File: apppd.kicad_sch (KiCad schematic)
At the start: 0 parts

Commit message: Added basic components from GPS
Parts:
- added C1, C9: 10uF, Resistor_SMD:R_0805_2012Metric_Pad1.20x1.40mm_HandSolder, symbol Device:C
- added C10, C12, C4, C5, C6, C7, C8: 100nF, Resistor_SMD:R_0805_2012Metric_Pad1.20x1.40mm_HandSolder, symbol Device:C
- added C11, C2, C3: 1uF, Resistor_SMD:R_0805_2012Metric_Pad1.20x1.40mm_HandSolder, symbol Device:C
- added D1, D2: LED, Package_TO_SOT_SMD:SOT-23, symbol Device:LED
- added F1: 100mA Polyfuse, Capacitor_SMD:C_0603_1608Metric_Pad1.08x0.95mm_HandSolder, symbol Device:Polyfuse
- added FB1: FerriteBead, Capacitor_SMD:C_0603_1608Metric_Pad1.08x0.95mm_HandSolder, symbol Device:FerriteBead_Small
- added J1: Conn_SWD, Connector_PinHeader_2.54mm:PinHeader_1x04_P2.54mm_Vertical, symbol Connector_Generic:Conn_01x04
- added J4: 2601-1102, apppd:WAGO-2601-1102, symbol telemetry:2601-1102
- added J5: USB_C_Receptacle_USB2.0_16P, apppd:USB-C-SMD_TYPE-C-16PIN-2MD-073, symbol Connector:USB_C_Receptacle_USB2.0_16P
- added Q1, Q2: AO3400A, Package_TO_SOT_SMD:SOT-23, symbol Transistor_FET:AO3400A
- added R1: 10k, Resistor_SMD:R_0805_2012Metric_Pad1.20x1.40mm_HandSolder, symbol Device:R
- added R10, R7, R8, R9: R_US, Resistor_THT:R_Array_SIP4, symbol Device:R_US
- added R2, R3: 5.1k, Resistor_SMD:R_0805_2012Metric_Pad1.20x1.40mm_HandSolder, symbol Device:R
- added R4, R5, R6: 10k, Resistor_SMD:R_0805_2012Metric_Pad1.20x1.40mm_HandSolder, symbol Device:R_US
- added SW1: NRST, apppd:SW-SMD_L3.9-W3.0-P4.45, symbol EasyEDA:TS-1088-AR02016
- added SW2: BOOT0, apppd:SW-SMD_L3.9-W3.0-P4.45, symbol EasyEDA:TS-1088-AR02016
- added TP5: CAN+, TestPoint:TestPoint_THTPad_D2.0mm_Drill1.0mm, symbol Connector:TestPoint
- added TP6: CAN-, TestPoint:TestPoint_THTPad_D2.0mm_Drill1.0mm, symbol Connector:TestPoint
- added TP7: +3V3, TestPoint:TestPoint_THTPad_D2.0mm_Drill1.0mm, symbol Connector:TestPoint
- added TP8: VIN_LDO, TestPoint:TestPoint_THTPad_D2.0mm_Drill1.0mm, symbol Connector:TestPoint
- added TP9: GND, TestPoint:TestPoint_THTPad_D2.0mm_Drill1.0mm, symbol Connector:TestPoint
- added U1: AP2112K-3.3, Package_TO_SOT_SMD:SOT-23-5_HandSoldering, symbol Regulator_Linear:AP2112K-3.3
- added U2: STM32F072CBTx, Package_QFP:LQFP-48_7x7mm_P0.5mm, symbol MCU_ST_STM32F0:STM32F072CBTx
- added U3: USBLC6-2SC6, Package_TO_SOT_SMD:SOT-23-6, symbol Power_Protection:USBLC6-2SC6
- added U4: TCAN337, Package_SO:SOIC-8_3.9x4.9mm_P1.27mm, symbol Interface_CAN_LIN:TCAN337
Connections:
- new net: J5.A5 (CC1), R2.1
- new net: J5.B5 (CC2), R3.1
- new net: FB1.2, U2.9 (VDDA)
- new net +3V3: C11.1, C12.2, C3.1, C4.2, C5.2, C6.2, C7.2, C8.2, C9.2, FB1.1, J1.4 (Pin_4), R4.1, R5.1, SW2.1, TP7.1, U1.5 (VOUT), U2.1 (VBAT), U2.24 (VDD), U2.36 (VDDIO2), U2.48 (VDD), U4.3 (VCC)
- new net BOOT0: R1.2, SW2.2, U2.44 (BOOT0)
- new net CAN+: J4.1 (1_1), J4.2 (1_2), TP5.1, U4.7 (CANH)
- new net CAN-: J4.3 (2_1), J4.4 (2_2), TP6.1, U4.6 (CANL)
- new net D+: U2.33 (PA12), U3.4 (I/O2)
- new net D-: U2.32 (PA11), U3.6 (I/O1)
- new net ETB_FET: U2.21 (PB10)
- new net FLT_CAN: R5.2, U2.18 (PB0), U4.5 (FAULT)
- new net GND: C1.1, C10.1, C11.2, C12.1, C2.2, C3.2, C4.1, C5.1, C6.1, C7.1, C8.1, C9.1, J1.1 (Pin_1), J5.A1 (GND), J5.A12 (GND), J5.B1 (GND), J5.B12 (GND), J5.SH (SHIELD), R1.1, R2.2, R3.2, R6.2, SW1.1, TP9.1, U1.2 (GND), U2.23 (VSS), U2.35 (VSS), U2.47 (VSS), U2.8 (VSSA), U3.2 (GND), U4.2 (GND)
- new net IGN_FET: U2.22 (PB11)
- new net NRST: C10.2, SW1.2, U2.7 (NRST)
- new net RXD_CAN: U2.45 (PB8), U4.4 (RXD)
- new net SIL_CAN: R6.1, U2.19 (PB1), U4.8 (S)
- new net SWCLK: J1.2 (Pin_2), U2.37 (PA14)
- new net SWDIO: J1.3 (Pin_3), U2.34 (PA13)
- new net TXD_CAN: R4.2, U2.46 (PB9), U4.1 (TXD)
- new net VBUS: F1.1, J5.A4 (VBUS), J5.A9 (VBUS), J5.B4 (VBUS), J5.B9 (VBUS), U3.5 (VBUS)
- new net VIN_LDO: C1.2, C2.1, F1.2, TP8.1, U1.1 (VIN), U1.3 (EN)
- new net inD+: J5.A6 (D+), J5.B6 (D+), U3.3 (I/O2)
- new net inD-: J5.A7 (D-), J5.B7 (D-), U3.1 (I/O1)
- no-connect marks 0 -> 24
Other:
- note added: "100nF for each other 3V3 pin"
- note added: "1uF and 100nF for VDDA"
- note added: "CAN Transciver"
- note added: "Clutch Position Data over CAN"
- note added: "Ignition and ETB Switching"
- note added: "Linear Voltage Regulator"
- note added: "Microcontroller Decoupling"
- note added: "STM32F0 MicroController"
- note added: "SWD Headers DEBUG/PROG"
- note added: "USB 2.0 Type C"
- note added: "check if 5V if 12V then use divider"

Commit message: Added buck converter, FETs and indication LEDs. Near complete
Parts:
- removed C4: 100nF, Resistor_SMD:R_0805_2012Metric_Pad1.20x1.40mm_HandSolder, symbol Device:C
- removed D1, D2: LED, Package_TO_SOT_SMD:SOT-23, symbol Device:LED
- added C13, C14: 8pF, Capacitor_SMD:C_0805_2012Metric_Pad1.18x1.45mm_HandSolder, symbol Device:C
- added C15, C24: 10uF, Capacitor_SMD:C_0805_2012Metric_Pad1.18x1.45mm_HandSolder, symbol Device:C
- added C16: 220nF, Capacitor_SMD:C_0805_2012Metric_Pad1.18x1.45mm_HandSolder, symbol Device:C
- added C17, C23: 1uF, Capacitor_SMD:C_0805_2012Metric_Pad1.18x1.45mm_HandSolder, symbol Device:C
- added C18: 100nF, Capacitor_SMD:C_0805_2012Metric_Pad1.18x1.45mm_HandSolder, symbol Device:C
- added C19, C20: 22uF, Capacitor_SMD:C_0805_2012Metric_Pad1.18x1.45mm_HandSolder, symbol Device:C
- added D1: BZT52-C15S-AU_R1_000A1, Diode_SMD:D_SOD-323_HandSoldering, symbol Device:D_Zener
- added D10, D11: PMEG2010BER, Diode_SMD:Nexperia_CFP3_SOD-123W, symbol Diode:PMEG2010BER
- added D2: SMBJ26A, Diode_SMD:D_SMA-SMB_Universal_Handsoldering, symbol Device:D_TVS
- added D3, D5: LED, apppd:AP2012EC, symbol Device:LED
- added D7, D8: S1B-13-F, apppd:S1B-13-F, symbol apppd:S1B-13-F
- added J2: APPPD Connector, apppd:MOLEX_430450800, symbol Connector_Generic:Conn_02x04_Counter_Clockwise
- added L1: 8.2uH, 86m, Inductor_SMD:L_Vishay_IHLP-1616, symbol Device:L
- added LED1: XL-2012SURUGC, apppd:XL-2012SURUGC, symbol apppd:XL-2012SURUGC
- added Q3: PMV100EPA, Package_TO_SOT_SMD:TSOT-23_HandSoldering, symbol Transistor_FET:DMP3099L
- added R11, R15: 100k, Resistor_SMD:R_0805_2012Metric_Pad1.20x1.40mm_HandSolder, symbol Device:R_US
- added R12: 24.9k, Resistor_SMD:R_0805_2012Metric_Pad1.20x1.40mm_HandSolder, symbol Device:R_US
- added R14, R19: 150, Resistor_SMD:R_0805_2012Metric_Pad1.20x1.40mm_HandSolder, symbol Device:R_US
- added R20: 470, Resistor_SMD:R_0805_2012Metric_Pad1.20x1.40mm_HandSolder, symbol Device:R_US
- added R21, R22: 1k, Resistor_SMD:R_0805_2012Metric_Pad1.20x1.40mm_HandSolder, symbol Device:R_US
- added U6: LMR33610ADDAR, Package_SO:Texas_HSOP-8-1EP_3.9x4.9mm_P1.27mm_ThermalVias, symbol Regulator_Switching:LMR33610ADDAR
- added Y1: ABM8AIG-24.000MHz-8-2Z-T, apppd:ABM8AIG-24.000MHZ-8-2Z-T, symbol telemetry:ABM8AIG-24.000MHz-8-2Z-T
- C1, C10, C11, C12, C2, C3, C5, C6, C7, C8, C9: footprint Resistor_SMD:R_0805_2012Metric_Pad1.20x1.40mm_HandSolder -> Capacitor_SMD:C_0805_2012Metric_Pad1.18x1.45mm_HandSolder
- F1: value 100mA Polyfuse -> 300mA Polyfuse; footprint Capacitor_SMD:C_0603_1608Metric_Pad1.08x0.95mm_HandSolder -> Fuse:Fuse_0805_2012Metric_Pad1.15x1.40mm_HandSolder
- R10, R9: value R_US -> 100k; footprint Resistor_THT:R_Array_SIP4 -> Resistor_SMD:R_0805_2012Metric_Pad1.20x1.40mm_HandSolder
- R7: value R_US -> 150; footprint Resistor_THT:R_Array_SIP4 -> Resistor_SMD:R_0805_2012Metric_Pad1.20x1.40mm_HandSolder
- R8: value R_US -> 10K; footprint Resistor_THT:R_Array_SIP4 -> Resistor_SMD:R_0805_2012Metric_Pad1.20x1.40mm_HandSolder
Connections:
- net +3V3: now also LED1.2 (+), LED1.4 (+)
- net APPS1: now also U2.10 (PA0), J2.5 (Pin_5)
- net APPS2: now also U2.11 (PA1), J2.6 (Pin_6)
- net GND: now also Q1.2 (S), Q2.2 (S), R8.2, R9.1, C13.2, C14.2, C15.2, C16.2, C17.2, C19.2, C20.2, C23.2, C24.1, D2.2 (A2), J2.4 (Pin_4), R12.2, R15.1, U6.1 (GND), U6.9 (GND), Y1.2 (GND), Y1.4 (GND)
- net LED1: now also U2.25 (PB12), R19.1
- net LED2: now also U2.26 (PB13), R20.1
- net TPS1: now also U2.12 (PA2), J2.7 (Pin_7)
- net TPS2: now also U2.13 (PA3), J2.8 (Pin_8)
- net at R9.2: now also Q1.1 (G), R7.2
- net PG: now reaches R10.1
- net PG: now also U6.4 (PG)
- net buckVCC: now reaches R10.2
- net buckVCC: now also C17.1, U6.6 (VCC)
- net at R8.1: now also D1.2 (A), Q3.1 (G)
- net IGN_IN: now reaches Q1.3 (D)
- net IGN_IN: now also D7.2 (A), J2.1 (Pin_1), R21.1
- net at Q2.1 (G): now also R14.2, R15.2
- net ETB_IN: now reaches Q2.3 (D)
- net ETB_IN: now also D8.2 (A), J2.2 (Pin_2), R22.1
- net IGN_CUT: now reaches R7.1
- net IGN_CUT: now also U2.20 (PB2)
- net ETB_CUT: now reaches U2.39 (PB3)
- net ETB_CUT: now also R14.1
- net CYST_IN: now reaches U2.5 (PF0)
- net CYST_IN: now also C14.1, Y1.1
- net CYST_OUT: now reaches U2.6 (PF1)
- net CYST_OUT: now also C13.1, Y1.3
- net VDDA: now reaches FB1.2, U2.9 (VDDA)
- net VDDA: now also C23.1, C24.2
- net VBUS: no longer names the net of J5.A4 (VBUS), J5.A9 (VBUS), J5.B4 (VBUS), J5.B9 (VBUS), U3.5 (VBUS)
- net VBUS: now also D10.2 (A); no longer F1.1
- new net: D5.1 (K), R22.2
- new net: C18.1, U6.7 (BOOT)
- new net: D3.1 (K), R21.2
- new net: C19.1, C20.1, D11.2 (A), L1.2, R11.1
- new net: LED1.1 (-), R19.2
- new net: LED1.3 (-), R20.2
- new net +12V: D2.1 (A1), D3.2 (A), D5.2 (A), D7.1 (K), D8.1 (K), J2.3 (Pin_3), Q3.3 (D)
- new net +5V: D10.1 (K), D11.1 (K), F1.1
- new net FB: R11.2, R12.1, U6.5 (FB)
- new net SW: C18.2, L1.1, U6.8 (SW)
- new net buckIN: C15.1, C16.1, D1.1 (K), Q3.2 (S), U6.2 (VIN), U6.3 (EN)
- no-connect marks 24 -> 19
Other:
- note added: "APPPD Connector"
- note added: "For debugging or indication"
- note added: "HSE Crystal"
- note added: "Reverse Polarity Protection and TVS"
- note added: "SMPS"
- note added: "power needs work"
- note removed: "check if 5V if 12V then use divider"
- moved on the sheet: C11, C12, C5, C6, C7, C8, C9, F1, FB1, J4, J5, Q1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

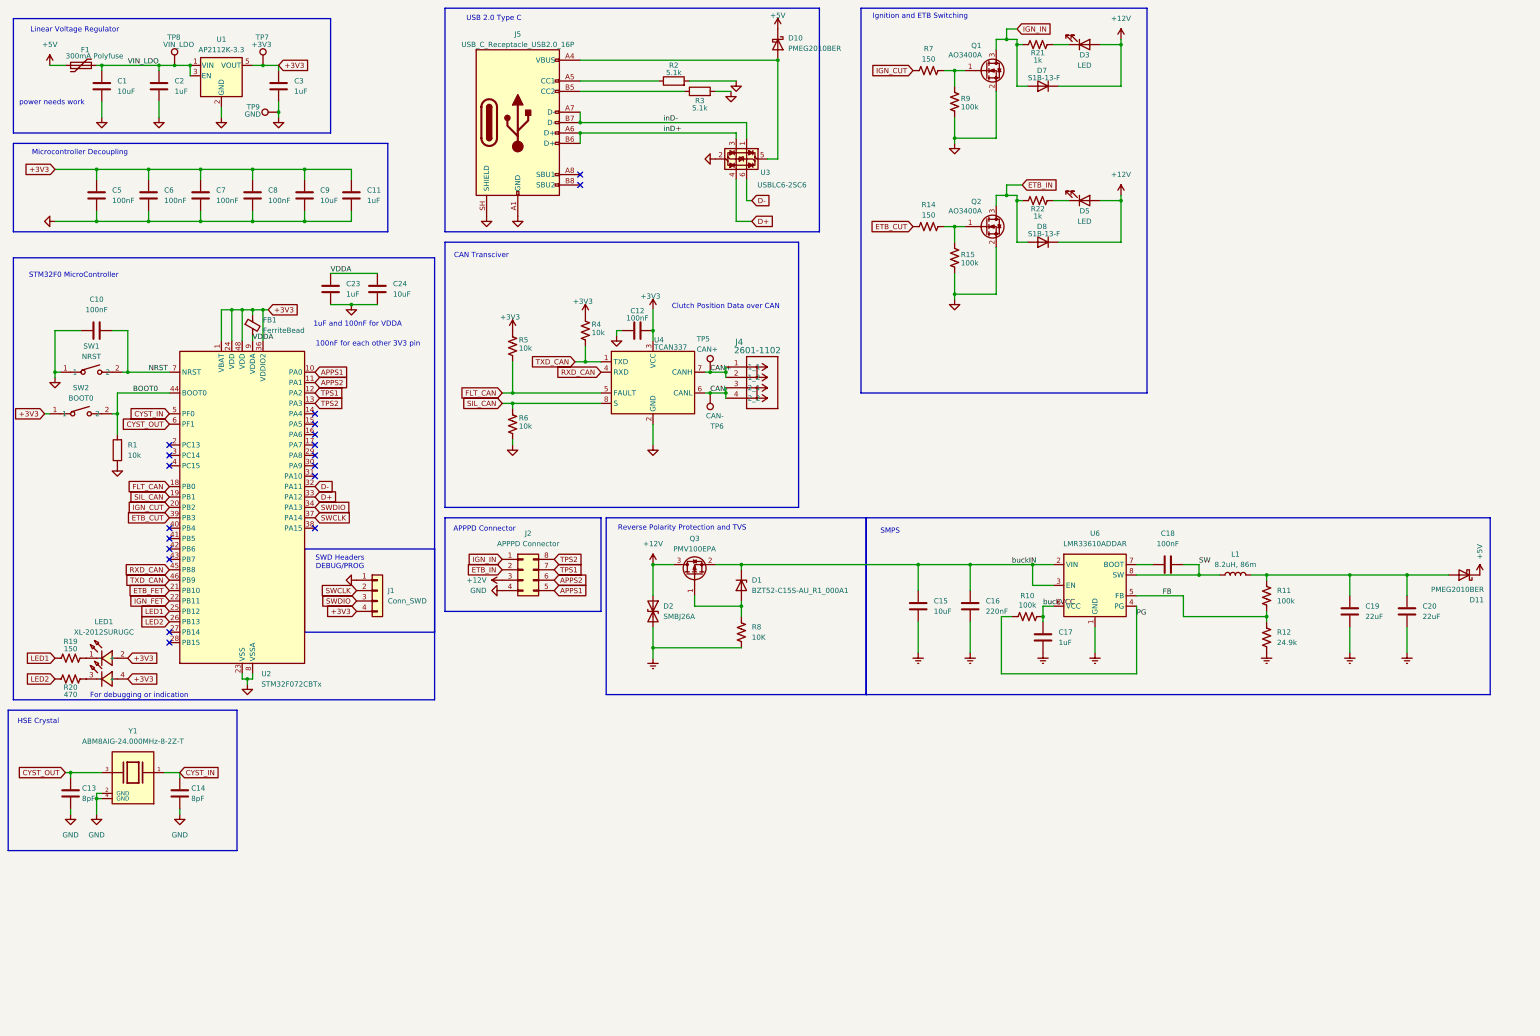
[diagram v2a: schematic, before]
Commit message: Voltage shift for apps and tps sensors, 3v3 compatability
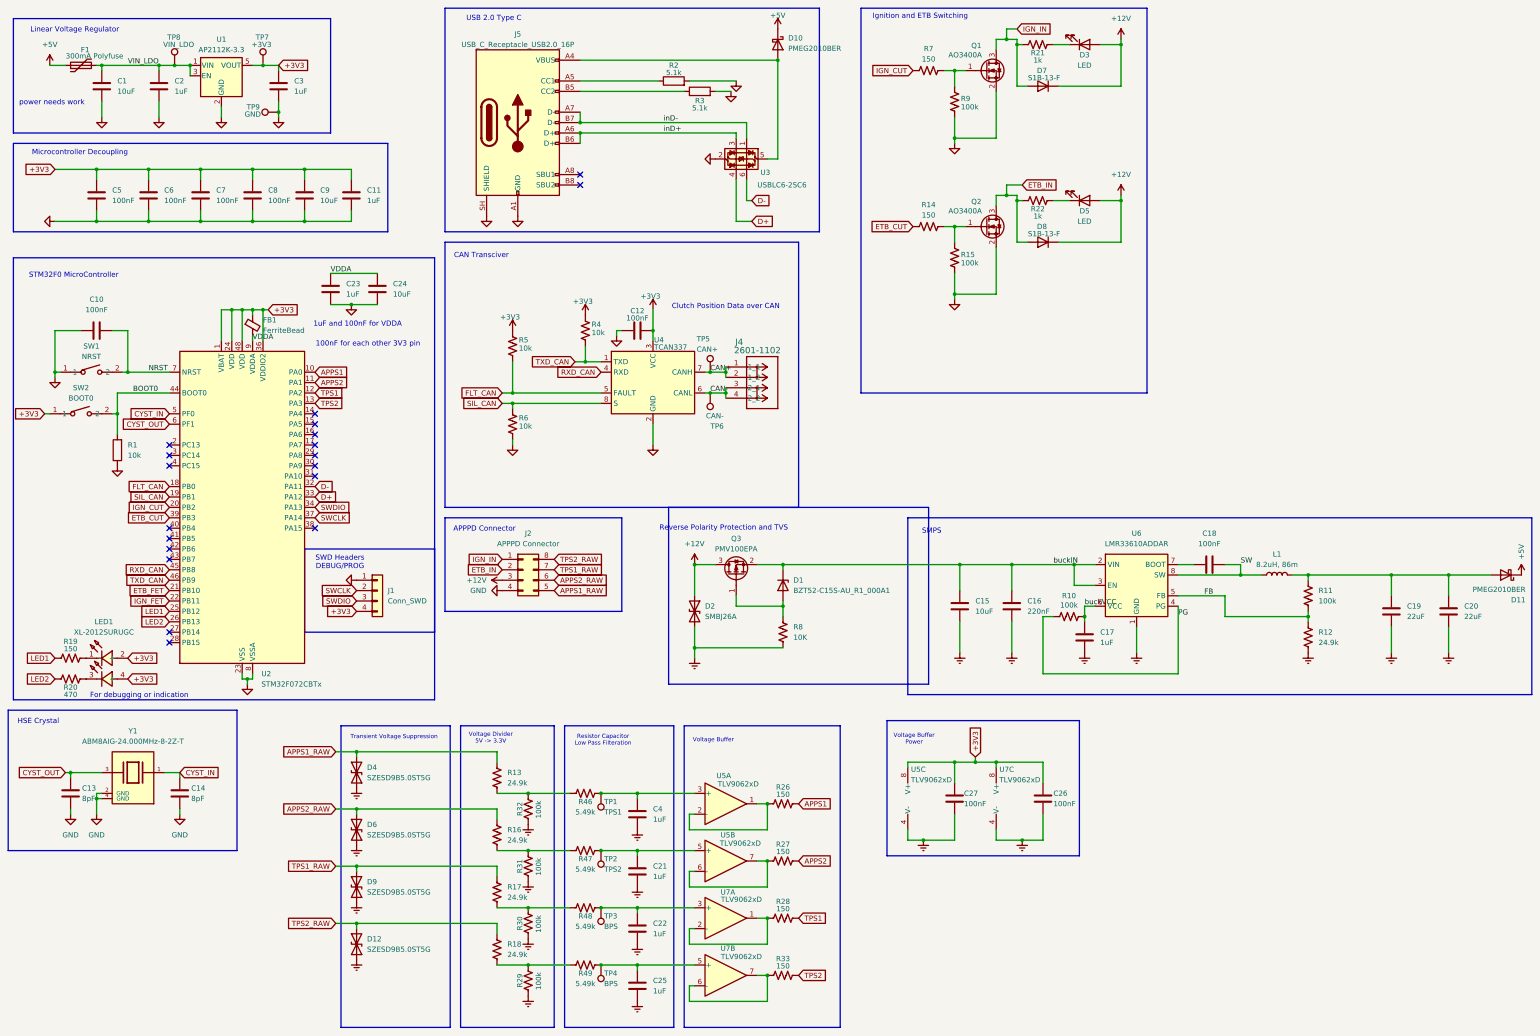
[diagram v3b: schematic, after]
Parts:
- added C21, C22, C25, C4: 1uF, Capacitor_SMD:C_0805_2012Metric_Pad1.18x1.45mm_HandSolder, symbol Device:C
- added C26, C27: 100nF, Capacitor_SMD:C_0805_2012Metric_Pad1.18x1.45mm_HandSolder, symbol Device:C
- added D12, D4, D6, D9: SZESD9B5.0ST5G, Diode_SMD:D_SOD-923, symbol Diode:SZESD9B5.0ST5G
- added R13, R16, R17, R18: 24.9k, Resistor_SMD:R_0805_2012Metric_Pad1.20x1.40mm_HandSolder, symbol Device:R_US
- added R26, R27, R28, R33: 150, Resistor_SMD:R_0805_2012Metric_Pad1.20x1.40mm_HandSolder, symbol Device:R_US
- added R29, R30, R31, R32: 100k, Resistor_SMD:R_0805_2012Metric_Pad1.20x1.40mm_HandSolder, symbol Device:R_US
- added R46, R47, R48, R49: 5.49k, Resistor_SMD:R_0805_2012Metric_Pad1.20x1.40mm_HandSolder, symbol Device:R_US
- added TP1: TPS1, TestPoint:TestPoint_Keystone_5000-5004_Miniature, symbol Connector:TestPoint
- added TP2: TPS2, TestPoint:TestPoint_Keystone_5000-5004_Miniature, symbol Connector:TestPoint
- added TP3, TP4: BPS, TestPoint:TestPoint_Keystone_5000-5004_Miniature, symbol Connector:TestPoint
- added U5, U7: TLV9062xD, Package_SO:SOIC-8_3.9x4.9mm_P1.27mm, symbol Amplifier_Operational:TLV9062xD
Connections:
- net +3V3: now also C26.2, C27.2, U5.8 (V+), U7.8 (V+)
- net APPS1: now also R26.2; no longer J2.5 (Pin_5)
- net APPS2: now also R27.2; no longer J2.6 (Pin_6)
- net TPS1: now also R28.2; no longer J2.7 (Pin_7)
- net TPS2: now also R33.2; no longer J2.8 (Pin_8)
- new net: C25.1, R49.2, TP4.1, U7.5 (+)
- new net: R16.2, R31.2, R47.1
- new net: C21.1, R47.2, TP2.1, U5.5 (+)
- new net: C4.1, R46.2, TP1.1, U5.3 (+)
- new net: R13.2, R32.2, R46.1
- new net: R33.1, U7.6 (-), U7.7
- new net: C22.1, R48.2, TP3.1, U7.3 (+)
- new net: R28.1, U7.1, U7.2 (-)
- new net: R27.1, U5.6 (-), U5.7
- new net: R18.2, R29.2, R49.1
- new net: R26.1, U5.1, U5.2 (-)
- new net: R17.2, R30.2, R48.1
- new net APPS1_RAW: D4.2 (A2), J2.5 (Pin_5), R13.1
- new net APPS2_RAW: D6.2 (A2), J2.6 (Pin_6), R16.1
- new net Earth: C21.2, C22.2, C25.2, C26.1, C27.1, C4.2, D12.1 (A1), D4.1 (A1), D6.1 (A1), D9.1 (A1), R29.1, R30.1, R31.1, R32.1, U5.4 (V-), U7.4 (V-)
- new net TPS1_RAW: D9.2 (A2), J2.7 (Pin_7), R17.1
- new net TPS2_RAW: D12.2 (A2), J2.8 (Pin_8), R18.1
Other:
- note added: "Resistor Capacitor Low Pass Filteration"
- note added: "Transient Voltage Suppression"
- note added: "Voltage Buffer"
- note added: "Voltage Buffer Power"
- note added: "Voltage Divider 5V -> 3.3V"
- moved on the sheet: C15, C16, C17, C18, C19, C20, D1, D11, D2, L1, Q3, R10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

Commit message: Fixed ground and small changes
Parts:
- removed R13, R16, R17, R18: 24.9k, Resistor_SMD:R_0805_2012Metric_Pad1.20x1.40mm_HandSolder, symbol Device:R_US
- added R34, R35, R36, R37: 100k, Resistor_SMD:R_0805_2012Metric_Pad1.20x1.40mm_HandSolder, symbol Device:R_US
- added R38, R39, R40, R41: 300k, Resistor_SMD:R_0805_2012Metric_Pad1.20x1.40mm_HandSolder, symbol Device:R_US
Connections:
- net APPS1_RAW: now also R34.2
- net APPS2_RAW: now also R35.2
- net Earth: now also R38.1, R39.1, R40.1, R41.1; no longer R29.1, R30.1, R31.1, R32.1
- net TPS1_RAW: now also R36.2
- net TPS2_RAW: now also R37.2
- net at R47.1: now also R31.1, R39.2; no longer R31.2
- net at R46.1: now also R32.1, R38.2; no longer R32.2
- net at R29.2: now also R37.1; no longer R49.1
- net at R48.1: now also R30.1, R40.2; no longer R30.2
- new net: R30.2, R36.1
- new net: R31.2, R35.1
- new net: R29.1, R41.2, R49.1
- new net: R32.2, R34.1

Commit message: Fixed GND net
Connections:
- net Earth is gone; now on net GND: C21.2, C22.2, C25.2, C26.1, C27.1, C4.2, D12.1 (A1), D4.1 (A1), D6.1 (A1), D9.1 (A1), R38.1, R39.1, R40.1, R41.1, U5.4 (V-), U7.4 (V-)
- net ETB_FET: now also R14.1
- net IGN_FET: now also R7.1
- net ETB_CUT: no longer names the net of U2.39 (PB3)
- net ETB_CUT: no longer R14.1
- net IGN_CUT: no longer names the net of U2.20 (PB2)
- net IGN_CUT: no longer R7.1
- no-connect marks 19 -> 21
